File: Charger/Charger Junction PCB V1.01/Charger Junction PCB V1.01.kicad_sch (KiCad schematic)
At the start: 12 parts, among them J2 12V Battery, J3 Charger, J4 J1772 Plug, J5 Power Switch, J7 E-Stop, SW1 J1772 Dummy Enable (BMS Overr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

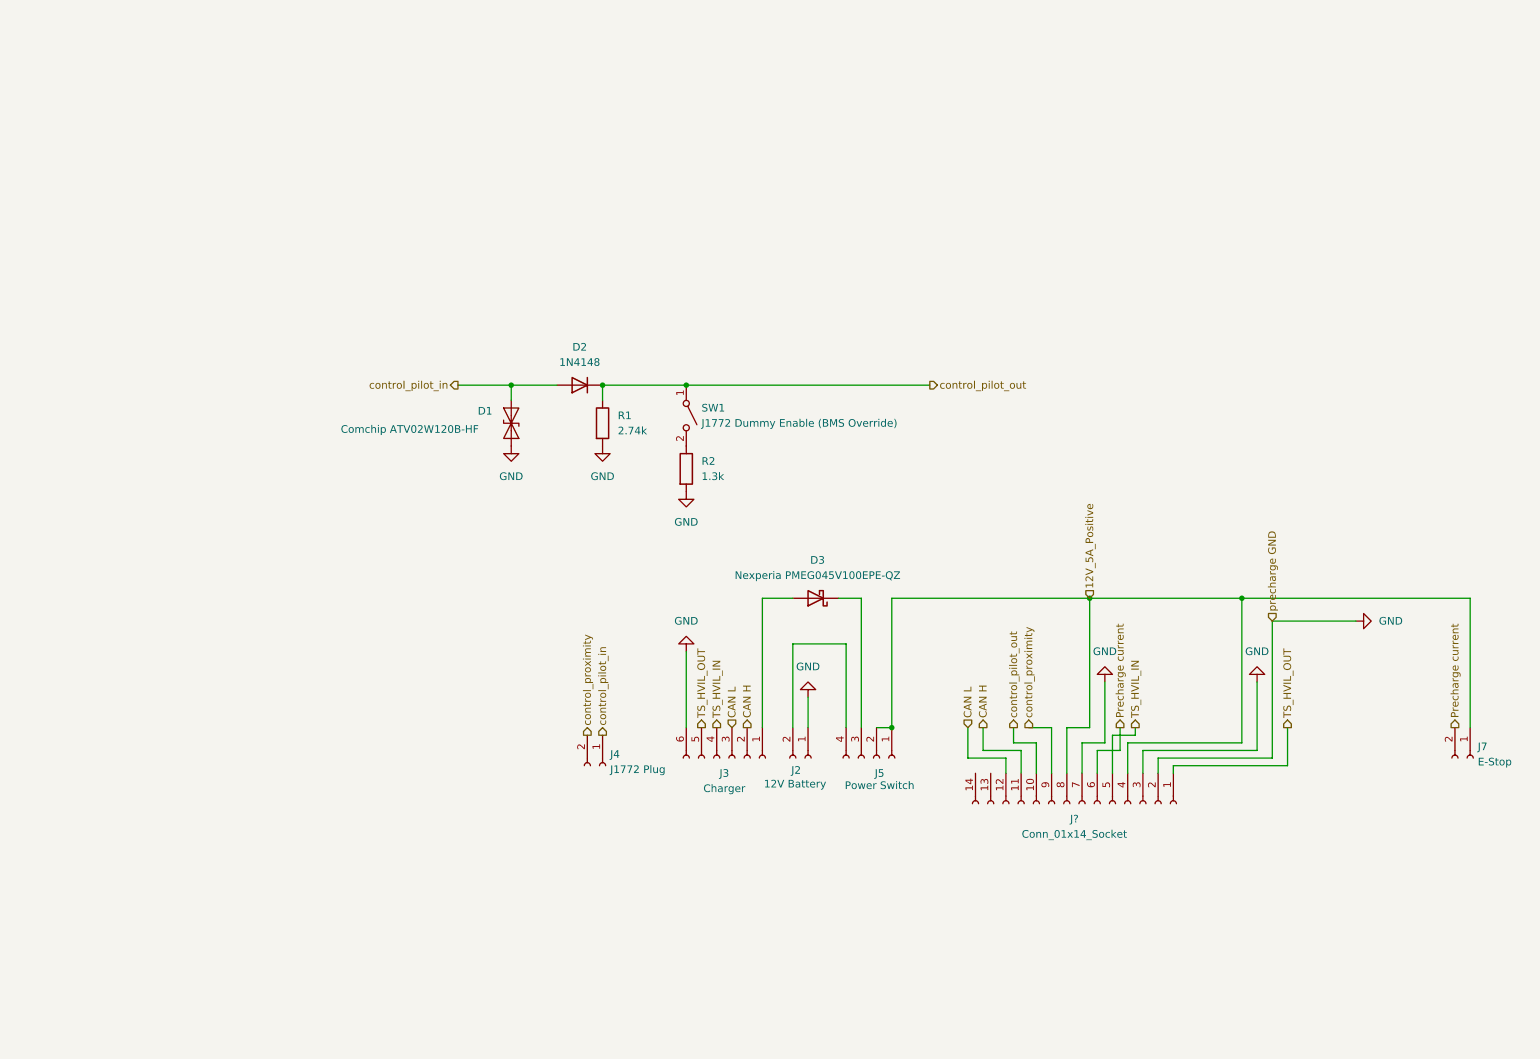
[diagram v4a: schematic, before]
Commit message: Added BMS and IMD shutdown latching circuit
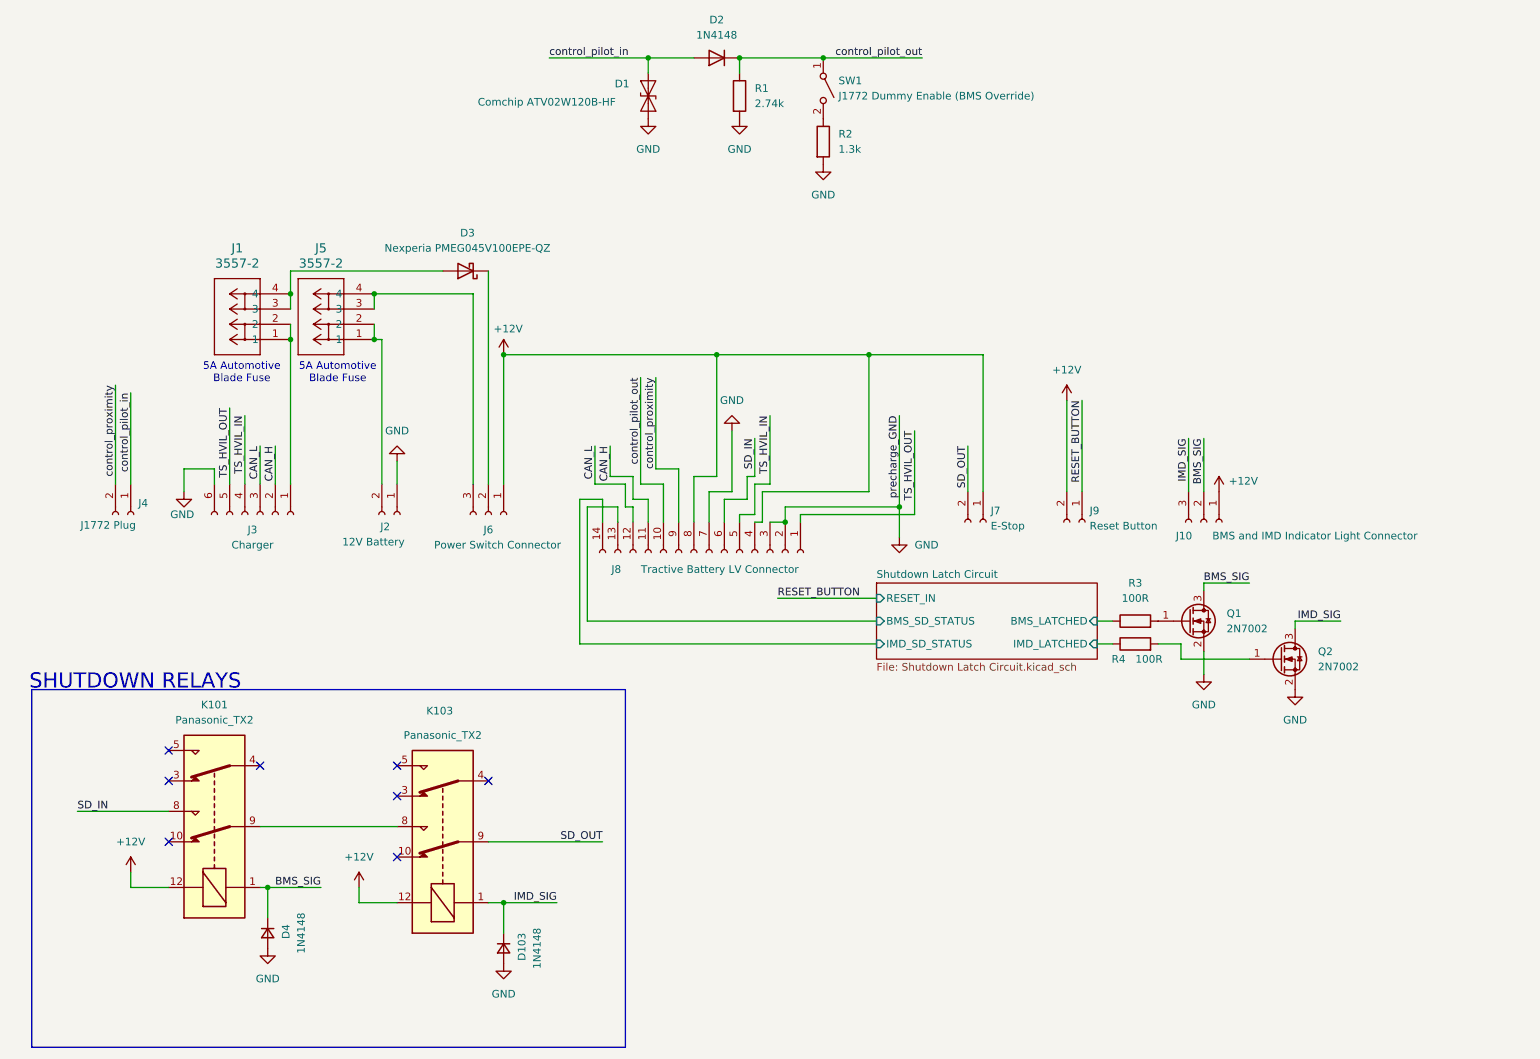
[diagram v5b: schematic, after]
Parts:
- removed J5: Power Switch, symbol Connector:Conn_01x04_Socket
- added D103, D4: 1N4148, Diode_SMD:D_0805_2012Metric_Pad1.15x1.40mm_HandSolder, symbol Device:D_Small
- added J1, J5: 3557-2, Keystone 3557-2 Fuse Holder:CONN_3557-2_KEY, symbol Keystone 3557-2 Fuse Holder:3557-2
- added J10: BMS and IMD Indicator Light Connector, symbol Connector:Conn_01x03_Socket
- added J6: Power Switch Connector, symbol Connector:Conn_01x03_Socket
- added J9: Reset Button, symbol Connector:Conn_01x02_Socket
- added K101, K103: Panasonic_TX2, JBox:Relay_DPDT_Panasonic_TXSA, symbol junction_pcb:Panasonic_TX2
- added Q1, Q2: 2N7002, Package_TO_SOT_SMD:SOT-23, symbol Transistor_FET:2N7002
- added R3, R4: 100R, symbol Device:R
- J8: renamed from J?; value Conn_01x14_Socket -> Tractive Battery LV Connector
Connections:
- net GND: now also D103.2 (A), D4.2 (A), Q1.2 (S), Q2.2 (S)
- net at J2.2 (Pin_2): now also J5.1, J5.2
- net at D3.1 (K): now also J6.2 (Pin_2)
- net at J3.1 (Pin_1): now also J1.1, J1.2; no longer D3.2 (A)
- net Shutdown Latch Circuit/BMS_SD_STATUS: now reaches J8.13 (Pin_13)
- net Shutdown Latch Circuit/IMD_SD_STATUS: now reaches J8.14 (Pin_14)
- net 12V_5A_Positive renamed +12V
- net +12V: now also J10.1 (Pin_1), J6.1 (Pin_1), J9.2 (Pin_2), K101.12, K103.12
- net CAN H renamed CAN_H
- net CAN L renamed CAN_L
- net Precharge current renamed SD_IN
- net SD_IN: now also K101.8; no longer J7.2 (Pin_2)
- new net: Q2.1 (G), R4.2
- new net: D3.2 (A), J1.3, J1.4
- new net: Q1.1 (G), R3.2
- new net: K101.9, K103.8
- new net: J5.3, J5.4, J6.3 (Pin_3)
- new net BMS_SIG: D4.1 (K), J10.2 (Pin_2), K101.1, Q1.3 (D)
- new net IMD_SIG: D103.1 (K), J10.3 (Pin_3), K103.1, Q2.3 (D)
- new net RESET_BUTTON: J9.1 (Pin_1)
- new net SD_OUT: J7.2 (Pin_2), K103.9
- new net Shutdown Latch Circuit/BMS_LATCHED: R3.1
- new net Shutdown Latch Circuit/IMD_LATCHED: R4.1
- no-connect marks 0 -> 8
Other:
- added sheet Shutdown Latch Circuit (Shutdown Latch Circuit.kicad_sch)
- note added: "5A Automotive Blade Fuse"
- note added: "SHUTDOWN RELAYS"
- moved on the sheet: D1, D2, D3, J2, J3, J4, J7, J8, R1, R2, SW1

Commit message: Added footprints
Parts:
- removed D3: Nexperia PMEG045V100EPE-QZ, symbol Diode:B360
- removed K101, K103: Panasonic_TX2, JBox:Relay_DPDT_Panasonic_TXSA, symbol junction_pcb:Panasonic_TX2
- added CR1: PMEG045V100EPE-QZ, Charger PCB:SOT1289_CFP15_NEX, symbol PMEG045V100EPE-QZ:PMEG100V080ELPDZ
- added K1, K2: Panasonic_TX2, JBox:Relay_DPDT_Panasonic_TXSA, symbol junction_pcb:Panasonic_TX2
- D2: footprint (none) -> Diode_SMD:D_SOD-323
- R1, R2, R3, R4: footprint (none) -> Resistor_SMD:R_0805_2012Metric_Pad1.20x1.40mm_HandSolder
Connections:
- net +12V: now also K1.12, K2.12
- net BMS_SIG: now also K1.1
- net IMD_SIG: now also K2.1
- net SD_IN: now also K1.8
- net SD_OUT: now also K2.9
- net at J1.3, J1.4: now also CR1.1 (ANODE), CR1.2 (ANODE)
- net at J6.2 (Pin_2): now also CR1.3 (CATHODE)
- new net: K1.9, K2.8

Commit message: Added TVS diodes, fixed symbols and footprints
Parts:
- removed D103, D4: 1N4148, Diode_SMD:D_0805_2012Metric_Pad1.15x1.40mm_HandSolder, symbol Device:D_Small
- removed D2: 1N4148, Diode_SMD:D_SOD-323, symbol Diode:1N4148
- added D2, D3, D5: SBAS16HT1G, Diode_SMD:D_SOD-323_HandSoldering, symbol Charger PCB:SBAS16HT1G
- added D6, D7: VTVS5V0ASMF-HM3-08, Charger PCB:D_SMF, symbol Charger PCB:VTVS5V0ASMF-HM3-08
- K1, K2: footprint JBox:Relay_DPDT_Panasonic_TXSA -> Charger PCB:Relay_DPDT_Panasonic_TXSA
- renumbered CR1 to D4
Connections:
- net BMS_SIG: now also D2.1 (K)
- net GND: now also D2.2 (A), D5.2 (A), D6.2 (A), D7.2 (A)
- net IMD_SIG: now also D5.1 (K)
- net Shutdown Latch Circuit/BMS_SD_STATUS: now also D6.1 (K)
- net Shutdown Latch Circuit/IMD_SD_STATUS: now also D7.1 (K)
- net control_pilot_in: now also D3.2 (A)
- net control_pilot_out: now also D3.1 (K)

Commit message: Fixed TB connector (14pin -> 12pin)
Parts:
- removed J8: Tractive Battery LV Connector, symbol Connector:Conn_01x14_Socket
- added J?: Tractive Battery Connector, symbol Connector:Conn_01x12_Socket
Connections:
- net +12V: now also J?.4 (Pin_4)
- net CAN_H: now also J?.11 (Pin_11)
- net CAN_L: now also J?.12 (Pin_12)
- net GND: now also J?.2 (Pin_2), J?.3 (Pin_3)
- net SD_IN: now also J?.6 (Pin_6)
- net Shutdown Latch Circuit/BMS_SD_STATUS: now also J?.7 (Pin_7)
- net Shutdown Latch Circuit/IMD_SD_STATUS: now also J?.8 (Pin_8)
- net TS_HVIL_IN: now also J?.5 (Pin_5)
- net TS_HVIL_OUT: now also J?.1 (Pin_1)
- net control_pilot_out: now also J?.10 (Pin_10)
- net control_proximity: now also J?.9 (Pin_9)
